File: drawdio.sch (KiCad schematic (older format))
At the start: 20 parts, among them P1 CONN_01X01, P2 CONN_01X01, P3 CONN_01X01, P4 CONN_01X02, P5 CONN_01X01, P6 CONN_01X01, P7 CONN_01X01, P8 CONN_01X01, Q1 BC558, Q2 BC547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

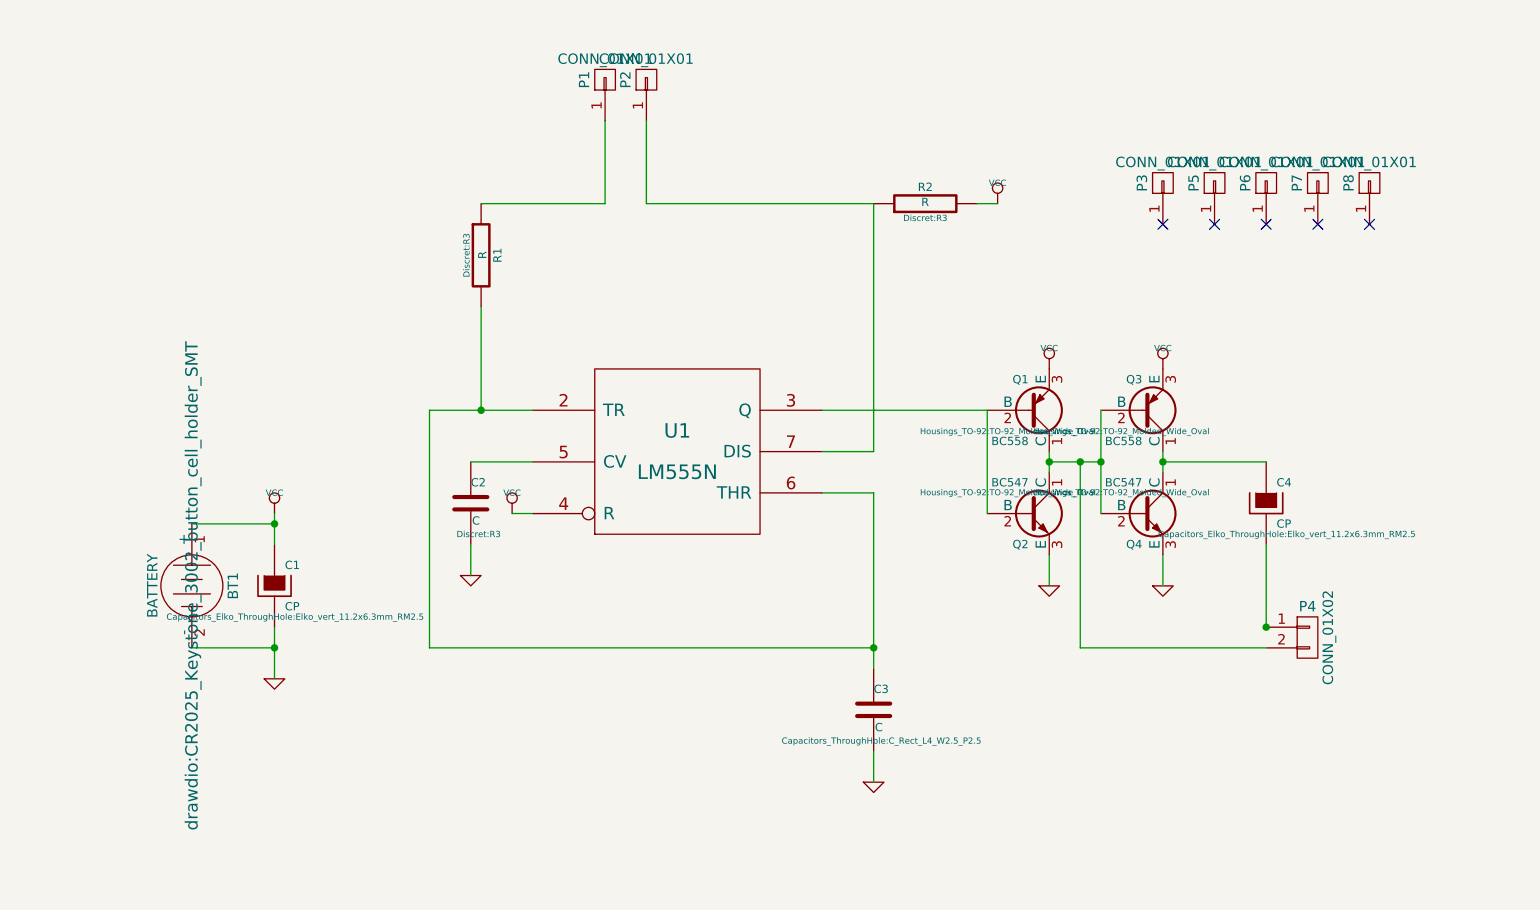
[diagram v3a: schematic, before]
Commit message: Añadidas resistencias
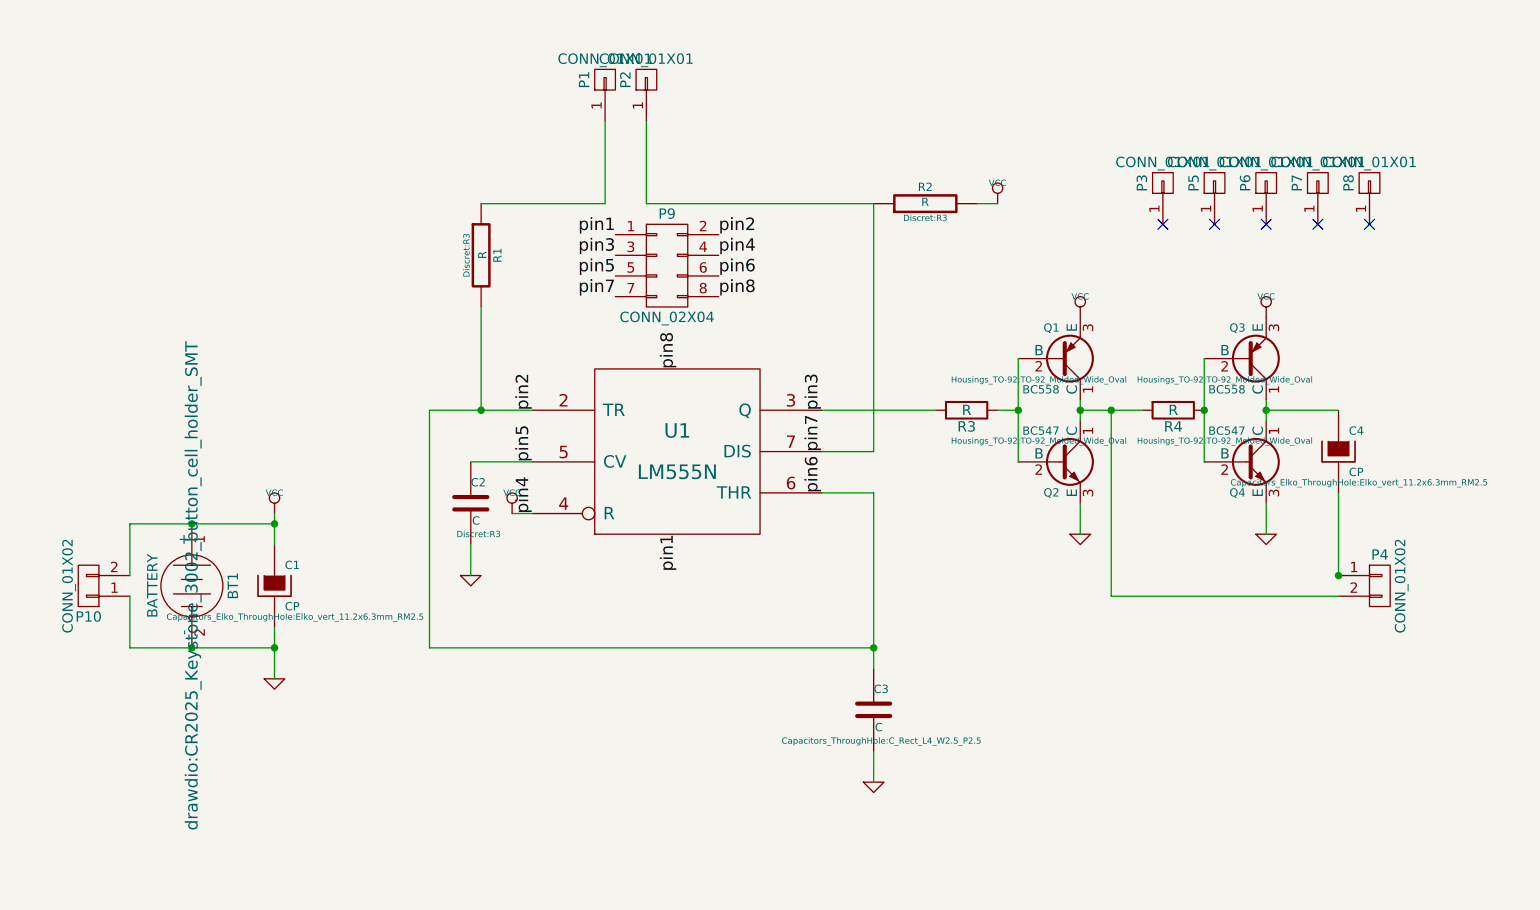
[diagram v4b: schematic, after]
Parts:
- added P10: CONN_01X02, drawdio:AAA_cell_holder, symbol CONN_01X02
- added P9: CONN_02X04, Housings_SOIC:SOIC-8_3.9x4.9mm_Pitch1.27mm, symbol CONN_02X04
- added R3, R4: R, Discret:R1, symbol R
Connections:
- net GND: now also P10.1 (P1), P9.1 (P1)
- net VCC: now also P10.2 (P2), P9.4 (P4), P9.8 (P8)
- net pin2: now reaches C3.1, R1.2, U1.2 (TR), U1.6 (THR)
- net pin2: now also P9.2 (P2), P9.6 (P6)
- net at Q1.2 (B), Q2.2 (B): now also R3.1; no longer U1.3 (Q)
- net pin5: now reaches C2.1, U1.5 (CV)
- net pin5: now also P9.5 (P5)
- net pin7: now reaches P2.1 (P1), R2.1, U1.7 (DIS)
- net pin7: now also P9.7 (P7)
- net at P4.2 (P2), Q1.1 (C), Q2.1 (C): now also R4.2; no longer Q3.2 (B), Q4.2 (B)
- new net: Q3.2 (B), Q4.2 (B), R4.1
- new net pin3: P9.3 (P3), R3.2, U1.3 (Q)
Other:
- moved on the sheet: C4, P4, Q1, Q2, Q3, Q4

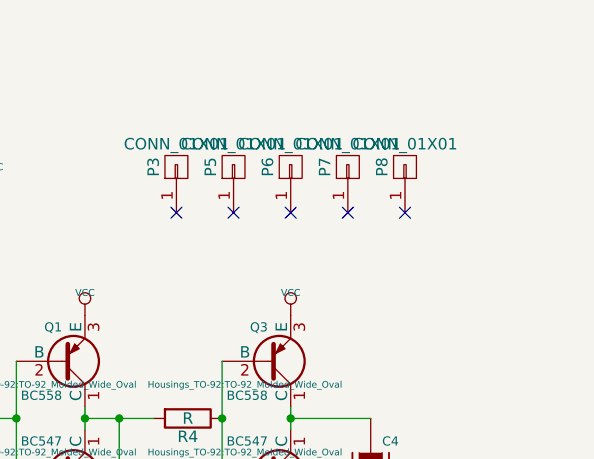
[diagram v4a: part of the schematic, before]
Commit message: AAA cell added
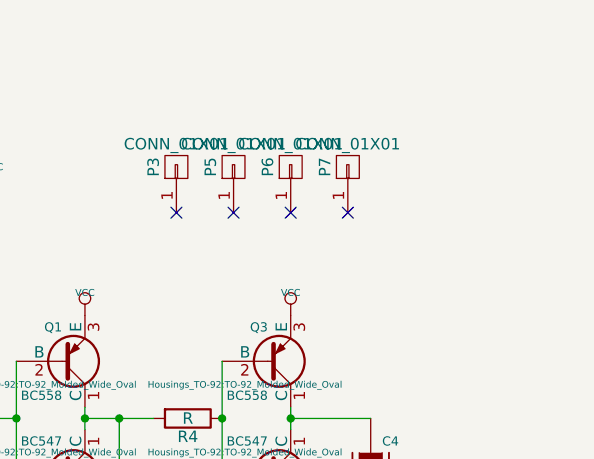
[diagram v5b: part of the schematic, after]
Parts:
- removed P8: CONN_01X01, drawdio:Symbol_OSHW-Logo_SilkScreen_BIG, symbol CONN_01X01
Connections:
- no-connect marks 5 -> 4
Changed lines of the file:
@@
 NoConn ~ 8450 2850
 NoConn ~ 8700 2850
-$Comp
-L CONN_01X01 P8
-U 1 1 5624AD30
-P 8950 2650
-F 0 "P8" H 8950 2750 50  0000 C CNN
-F 1 "CONN_01X01" V 9050 2650 50  0000 C CNN
-F 2 "drawdio:Symbol_OSHW-Logo_SilkScreen_BIG" H 8950 2650 60  0001 C CNN
-F 3 "" H 8950 2650 60  0000 C CNN
-	1    8950 2650
-	0    -1   -1   0
-$EndComp
-NoConn ~ 8950 2850
 Wire Wire Line
 	4400 3750 4900 3750

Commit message: Wiki is coming
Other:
- note added: "Alimentación"
- note added: "Altavoz"
- note added: "Etapa de salida"
- note added: "Oscilador"
- note added: "Pads de contacto"
- note added: "Taladros mecánicos"
- note added: "footprint SMD"
- moved on the sheet: P4
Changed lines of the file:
@@
 LIBS:memory
 LIBS:xilinx
-LIBS:special
 LIBS:microcontrollers
 LIBS:dsp
@@
 encoding utf-8
 Sheet 1 1
-Title ""
+Title "Drawdio"
 Date "20 apr 2015"
-Rev ""
-Comp ""
-Comment1 ""
-Comment2 ""
+Rev "V1.0"
+Comp "UC3Music"
+Comment1 "Originally designed by Jay Silver"
+Comment2 "Upgrades on output stage by JorFru"
 Comment3 ""
 Comment4 ""
@@
 F 0 "Q3" H 8350 3351 40  0000 R CNN
 F 1 "BC558" H 8350 3650 40  0000 R CNN
-F 2 "Housings_TO-92:TO-92_Molded_Wide_Oval" H 8250 3602 29  0000 C CNN
+F 2 "Housings_TO-92:TO-92_Molded_Wide_Oval" H 7700 3600 29  0001 C CNN
 F 3 "" H 8350 3500 60  0000 C CNN
 	1    8350 3500
@@
 F 0 "C4" H 8850 4050 40  0000 L CNN
 F 1 "CP" H 8850 3850 40  0000 L CNN
-F 2 "Capacitors_Elko_ThroughHole:Elko_vert_11.2x6.3mm_RM2.5" H 8900 3800 30  0000 C CNN
+F 2 "Capacitors_Elko_ThroughHole:Elko_vert_11.2x6.3mm_RM2.5" H 8900 3800 30  0001 C CNN
 F 3 "~" H 8800 3950 300 0000 C CNN
 	1    8800 3950
@@
 F 0 "C3" H 6550 5300 40  0000 L CNN
 F 1 "C" H 6556 5115 40  0000 L CNN
-F 2 "Capacitors_ThroughHole:C_Rect_L4_W2.5_P2.5" H 6588 5050 30  0000 C CNN
+F 2 "Capacitors_ThroughHole:C_Rect_L4_W2.5_P2.5" H 6588 5050 30  0001 C CNN
 F 3 "~" H 6550 5200 60  0000 C CNN
 	1    6550 5200
@@
 F 0 "C1" H 3700 4700 40  0000 L CNN
 F 1 "CP" H 3700 4500 40  0000 L CNN
-F 2 "Capacitors_Elko_ThroughHole:Elko_vert_11.2x6.3mm_RM2.5" H 3750 4450 30  0000 C CNN
+F 2 "Capacitors_Elko_ThroughHole:Elko_vert_11.2x6.3mm_RM2.5" H 7850 5600 30  0001 C CNN
 F 3 "~" H 3650 4600 300 0000 C CNN
 	1    3650 4600
@@
 F 0 "BT1" H 3250 4800 50  0000 C CNN
 F 1 "BATTERY" H 3250 4410 50  0000 C CNN
-F 2 "drawdio:CR2025_Keystone_3002_button_cell_holder_SMT" H 3250 4600 60  0000 C CNN
+F 2 "drawdio:CR2025_Keystone_3002_button_cell_holder_SMT" H 3400 5350 60  0001 C CNN
 F 3 "~" H 3250 4600 60  0000 C CNN
 	1    3250 4600
@@
 F 0 "Q4" H 8350 3851 40  0000 R CNN
 F 1 "BC547" H 8350 4150 40  0000 R CNN
-F 2 "Housings_TO-92:TO-92_Molded_Wide_Oval" H 8250 4102 29  0000 C CNN
+F 2 "Housings_TO-92:TO-92_Molded_Wide_Oval" H 8250 4102 29  0001 C CNN
 F 3 "" H 8350 4000 60  0000 C CNN
 	1    8350 4000
@@
 F 0 "Q1" H 7450 3351 40  0000 R CNN
 F 1 "BC558" H 7450 3650 40  0000 R CNN
-F 2 "Housings_TO-92:TO-92_Molded_Wide_Oval" H 7350 3602 29  0000 C CNN
+F 2 "Housings_TO-92:TO-92_Molded_Wide_Oval" H 7350 3602 29  0001 C CNN
 F 3 "" H 7450 3500 60  0000 C CNN
 	1    7450 3500
@@
 F 0 "Q2" H 7450 3851 40  0000 R CNN
 F 1 "BC547" H 7450 4150 40  0000 R CNN
-F 2 "Housings_TO-92:TO-92_Molded_Wide_Oval" H 7350 4102 29  0000 C CNN
+F 2 "Housings_TO-92:TO-92_Molded_Wide_Oval" V 7350 4102 29  0001 C CNN
 F 3 "" H 7450 4000 60  0000 C CNN
 	1    7450 4000
@@
 L CONN_01X02 P4
 U 1 1 562400DE
-P 9000 4600
-F 0 "P4" H 9000 4750 50  0000 C CNN
-F 1 "CONN_01X02" V 9100 4600 50  0000 C CNN
-F 2 "drawdio:RS_mini_speaker_724-3100" H 9000 4600 60  0001 C CNN
-F 3 "" H 9000 4600 60  0000 C CNN
-	1    9000 4600
+P 9000 5050
+F 0 "P4" H 9000 5200 50  0000 C CNN
+F 1 "CONN_01X02" V 9100 5050 50  0000 C CNN
+F 2 "drawdio:RS_mini_speaker_724-3100" H 9000 5050 60  0001 C CNN
+F 3 "" H 9000 5050 60  0000 C CNN
+	1    9000 5050
 	1    0    0    -1
 $EndComp
@@
 Wire Wire Line
 	4600 4550 4600 4400
-Connection ~ 8800 4550
 Wire Wire Line
 	7550 4350 7550 4200
@@
 Connection ~ 8150 3750
 Wire Wire Line
-	8800 4150 8800 4550
+	8800 4150 8800 5000
 Wire Wire Line
 	8450 3700 8450 3800
 Connection ~ 8450 3750
 Wire Wire Line
-	7700 3750 7700 4650
-Wire Wire Line
-	7700 4650 8800 4650
+	7700 3750 7700 5100
+Wire Wire Line
+	7700 5100 8800 5100
 Connection ~ 7700 3750
 $Comp
@@
 P 5550 3050
 F 0 "P9" H 5550 3300 50  0000 C CNN
-F 1 "CONN_02X04" H 5550 2800 50  0000 C CNN
+F 1 "CONN_02X04" H 5550 2800 50  0001 C CNN
 F 2 "Housings_SOIC:SOIC-8_3.9x4.9mm_Pitch1.27mm" H 5550 1850 60  0001 C CNN
 F 3 "" H 5550 1850 60  0000 C CNN
@@
 	2950 4650 2950 4900
 Connection ~ 3250 4900
+Wire Notes Line
+	6800 3050 6800 4450
+Wire Notes Line
+	6800 4450 9050 4450
+Wire Notes Line
+	9050 4450 9050 3050
+Wire Notes Line
+	9050 3050 6800 3050
+Wire Notes Line
+	7700 2450 7700 2950
+Wire Notes Line
+	7700 2950 9000 2950
+Wire Notes Line
+	9000 2950 9000 2450
+Wire Notes Line
+	9000 2450 7700 2450
+Text Notes 8950 4800 0    60   ~ 0
+Altavoz
+Text Notes 7600 3150 0    60   ~ 0
+Etapa de salida
+Text Notes 7950 2450 0    60   ~ 0
+Taladros mecánicos
+Wire Notes Line
+	2400 4100 2400 5150
+Wire Notes Line
+	2400 5150 3800 5150
+Wire Notes Line
+	3800 5150 3800 4100
+Wire Notes Line
+	3800 4100 2400 4100
+Text Notes 2800 4000 0    60   ~ 0
+Alimentación
+Wire Notes Line
+	4900 1850 4900 2400
+Wire Notes Line
+	4900 2400 5850 2400
+Wire Notes Line
+	5850 2400 5850 1850
+Wire Notes Line
+	5850 1850 4900 1850
+Text Notes 5000 1950 0    60   ~ 0
+Pads de contacto
+Wire Notes Line
+	4250 2550 4250 5650
+Wire Notes Line
+	4250 5650 6700 5650
+Wire Notes Line
+	6700 5650 6700 2550
+Wire Notes Line
+	6700 2550 4250 2550
+Text Notes 4300 2500 0    60   ~ 0
+Oscilador
+Wire Notes Line
+	5050 2800 5050 3300
+Wire Notes Line
+	5050 3300 6050 3300
+Wire Notes Line
+	6050 3300 6050 2800
+Wire Notes Line
+	6050 2800 5050 2800
+Text Notes 5300 3300 0    60   ~ 0
+footprint SMD
 $EndSCHEMATC
